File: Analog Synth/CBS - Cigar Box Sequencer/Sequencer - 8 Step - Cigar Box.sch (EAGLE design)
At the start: 117 parts, among them IC1 TL084P, IC10 79L05, IC2 TL084P, IC3 TL084P, IC4 74AC138N, IC5 4050N, IC6 78L05, IC7 40193N, IC8 78L05, Q1 I/O, Q2 I/O, Q3 I/O, X1 I/O, X2 I/O, X3 I/O

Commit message: CBS - still working on Cigar Box Sequencer schematic
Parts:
- added IC9: 74LS86N, 74xx-us:74LS86N
- added Q4: 2N3906, transistor-pnp:2N3906
- added R19, R20, R21: 47k, rcl:R-US_R0603
- added R22, R23, R24, R25: 10k, rcl:R-US_R0603
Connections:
- new net -5V_LEDS: Q4.E
- new net INTERNAL_RESET: IC9B.I1
- new net N$41: Q4.B, R19.1, R20.2
- new net N$42: IC7G$1.CLEAR, IC9B.O
- new net N$43: IC5F.I, R21.1
- new net N$44: LED-INT-OSC.C, R22.2
- new net N$45: CLK-SOURCE.B1, IC5F.O, IC9A.I0, LED-INT-OSC.A
- new net N$46: CLK-SOURCE.A, CLK-SOURCE.B, IC9C.I0
- new net N$47: CLK-SOURCE.B2, IC9A.O
- new net N$48: CLK-SOURCE.A3, LED-EXTERNAL.A
- new net N$49: CLK-SOURCE.A2, LED-INT+EXT.A
- new net N$50: CLK-SOURCE.A1, LED-INTERNAL.A
- new net N$51: LED-INTERNAL.C, R23.2
- new net N$52: LED-INT+EXT.C, R24.2
- new net N$53: LED-EXTERNAL.C, R25.2
- new net N$54: R21.2
- new net N$55: IC7G$1.UP, IC9C.O
- new net N$56: IC9C.I1
- net +5V: now also FREQ-MANUAL.E
- net -12V: now also Q4.C, R20.1
- net -5V: now also FREQ-MANUAL.A
- net 5V_DIGITAL: now also IC7P.VDD, IC9P.VCC
- net GND: now also IC7G$1.A, IC7G$1.B, IC7G$1.C, IC7G$1.D, IC7G$1.LOAD, IC9P.GND, R19.2, R22.1, R23.1, R24.1, R25.1; no longer X1.P3, X2.P3, X3.P3
- net N$1: now also LED-FREQ-CV.A
- net N$10: now also IC9B.I0
- net N$25: now also CLK-SOURCE.B3, IC9A.I1
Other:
- moved on the sheet: C4, C5, CV-OUT, FREQ-CV, FREQ-MANUAL, FREQ-RANGE, IC1A, IC4, IC5F, IC7, IC7P, LED-EXTERNAL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

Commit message: CBS - still working through Cigar Box Sequencer details
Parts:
- added R26, R27, R30, R32: 1k, rcl:R-US_R0603
- added R31, R33, R34, R35: 10k, rcl:R-US_R0603
- R19: value 47k -> 33k
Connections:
- net N$11 renamed X3
- net N$23 renamed X2
- net N$24 renamed X1
- removed net -5V_LEDS: Q4.E
- new net LED_SUPPLY: LED-FREQ-CV.C, Q4.E
- new net N$11: Q1.P2, R26.2
- new net N$23: Q2.P2, R27.2
- new net N$24: Q3.P2, R30.2
- new net N$61: LED-CLK-OUT.C, R31.2
- new net N$62: LED-Q1.C, R33.2
- new net N$63: LED-Q2.C, R34.2
- new net N$64: LED-Q3.C, R35.2
- new net Q1: IC7G$1.QA, LED-Q1.A, R26.1, X1.P3
- new net Q2: IC7G$1.QB, LED-Q2.A, R27.1, X2.P3
- new net Q3: IC7G$1.QC, LED-Q3.A, R30.1, X3.P3
- net GND: now also CLK-OUT.P$1, Q1.P$1, Q2.P$1, Q3.P$1, R31.1, R33.1, R34.1, R35.1
- net N$55: now also LED-CLK-OUT.A, R32.1
- net N$56: now also CLK-OUT.P2, R32.2; no longer IC9C.I1
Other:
- moved on the sheet: CLK-IN, CLK-OUT, CLK-SOURCE, IC7, IC7P, IC9C, LED-EXTERNAL, LED-INT+EXT, LED-INTERNAL, Q1, Q2, Q3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

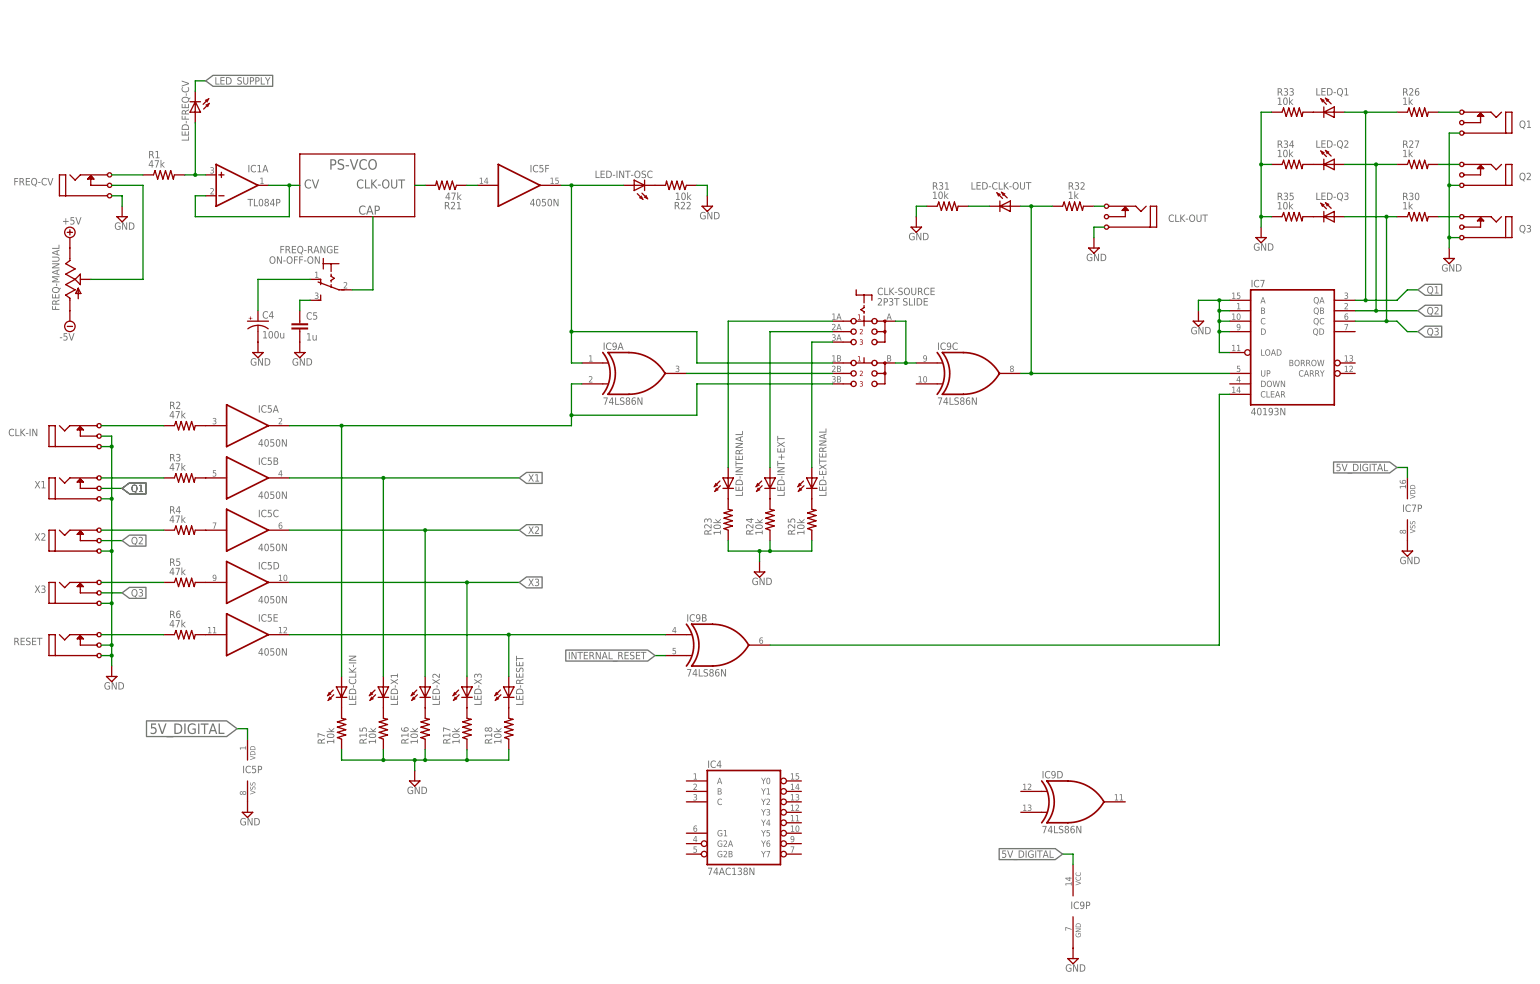
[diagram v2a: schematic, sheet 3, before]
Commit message: CBS: still working on schematic. I need to make sure I understand how I thought this was supposed to work BEFORE I start soldering things together
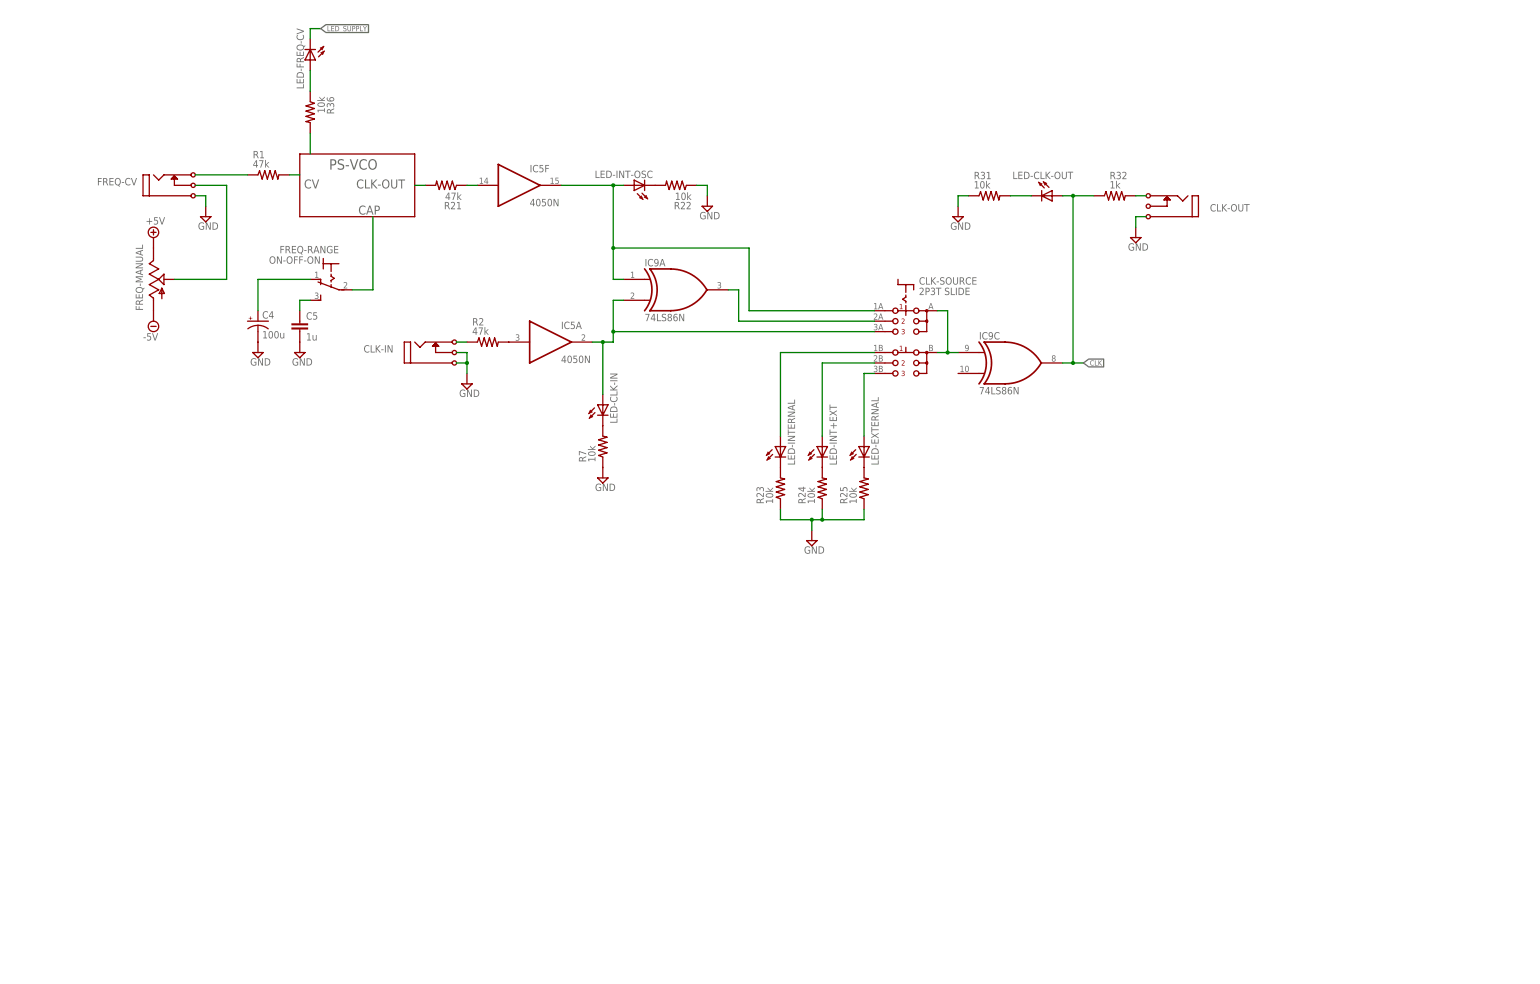
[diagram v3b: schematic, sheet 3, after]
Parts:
- added IC12: 74AC138N, 74xx-eu:74AC138N
- added IC13: 74ALS04N, 74xx-us:74ALS04N
- added R36, R37, R38, R39, R40, R41, R42, R43, R44: 10k, rcl:R-US_R0603
- added S11: STEP-DOWN, switch:5501
- added S9: STEP-UP, switch:5501
- IC4: value 74AC138N -> 74ALS04N; device 74xx-eu:74AC138N -> 74xx-us:74ALS04N
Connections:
- removed net 5V_DIGITAL: C2.+, C3.1, IC5P.VDD, IC6.OUT, IC7P.VDD, IC9P.VCC
- removed net N$47: CLK-SOURCE.B2, IC9A.O
- new net 5V_D: C2.+, C3.1, IC12A.G1, IC12P.VCC, IC13P.VCC, IC4P.VCC, IC5P.VDD, IC6.OUT, IC7P.VDD
- new net CLK: IC9C.O, IC9D.I0, LED-CLK-OUT.A, R32.1
- new net CLK_MAN_DOWN: IC7G$1.DOWN
- new net CLK_MAN_UP: IC9D.I1
- new net N$57: LED-FREQ-CV.A, R36.1
- new net N$58: IC12A.Y3, IC4D.I
- new net N$59: IC12A.Y4, IC4E.I
- new net N$60: IC12A.Y2, IC4C.I
- new net N$65: IC12A.Y1, IC4B.I
- new net N$66: IC12A.Y0, IC4A.I
- new net N$67: IC12A.Y5, IC4F.I
- new net N$68: IC12A.Y6, IC13A.I
- new net N$69: IC12A.Y7, IC13B.I
- new net N$70: CLK-SOURCE.A2, IC9A.O
- new net N$78: LED-S1.C, R37.2
- new net N$79: LED-S2.C, R38.2
- new net N$80: LED-S3.C, R39.2
- new net N$81: LED-S4.C, R40.2
- new net N$82: LED-S5.C, R41.2
- new net N$83: LED-S6.C, R42.2
- new net N$84: LED-S7.C, R43.2
- new net N$85: LED-S8.C, R44.2
- new net S1: IC4A.O, LED-S1.A
- new net S2: IC4B.O, LED-S2.A
- new net S3: IC4C.O, LED-S3.A
- new net S4: IC4D.O, LED-S4.A, S10.11
- new net S5: IC4E.O, LED-S5.A, S10.21
- new net S6: IC4F.O, LED-S6.A, S10.31
- new net S7: IC13A.O, LED-S7.A, S10.41
- new net S8: IC13B.O, LED-S8.A, S10.51
- net GND: now also IC12A.G2A, IC12A.G2B, IC12P.GND, IC13P.GND, IC4P.GND, R37.1, R38.1, R39.1, R40.1, R41.1, R42.1, R43.1, R44.1, S10.61; no longer IC9P.GND
- net INTERNAL_RESET: now also S10.S1
- net N$1: now also R36.2; no longer IC1A.+IN, LED-FREQ-CV.A, R1.2
- net N$25: now also CLK-SOURCE.A3; no longer CLK-SOURCE.B3
- net N$3: now also R1.2; no longer IC1A.-IN, IC1A.OUT
- net N$45: now also CLK-SOURCE.A1; no longer CLK-SOURCE.B1
- net N$48: now also CLK-SOURCE.B3; no longer CLK-SOURCE.A3
- net N$49: now also CLK-SOURCE.B2; no longer CLK-SOURCE.A2
- net N$50: now also CLK-SOURCE.B1; no longer CLK-SOURCE.A1
- net N$55: now also IC9D.O; no longer IC9C.O, LED-CLK-OUT.A, R32.1
- net X1: now also IC12A.A
- net X2: now also IC12A.B
- net X3: now also IC12A.C
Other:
- note added: "+5V Supply for Analog"
- note added: "-4.2 V Supply for LEDs"
- note added: "-5V Supply for Analog"
- note added: "Digital 5V Supply"
- moved on the sheet: C1, C2, C3, CLK-IN, CLK-OUT, CLK-SOURCE, FREQ-CV, FREQ-MANUAL, IC5A, IC6, IC9A, IC9C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

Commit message: CBS: working on skiimatic
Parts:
- removed R38, R39, R40, R41, R42, R43, R44: 10k, rcl:R-US_R0603
- removed S11: STEP-DOWN, switch:5501
- added C6: 0.1u, resistor:C-EU025-050X050
- added C7: 1n, resistor:C-EU025-050X050
- added IC11: MCP6002, linear:MCP602P
- added Q10, Q11, Q12, Q13, Q6, Q7, Q8, Q9: J310, transistor-small-signal:J310
- added Q5: 2N3904, transistor-npn:2N3904
- added R45, R48: 100k, resistor:R-US_0204/7
- added R46: 220k, resistor:R-US_0204/7
- added R47: 47k, resistor:R-US_0204/7
- added R49: 10k, resistor:R-US_0204/7
- added R50, R51, R52, R53, R54, R55, R56, R57: 1M, resistor:R-US_0204/7
- added R58, R59, R60, R61, R62, R63, R64, R65: 1k, resistor:R-US_0204/7
- added U$3: DIODE-0204/5, !synth_sch:DIODE-0204/5
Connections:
- removed net CLK_MAN_DOWN: IC7G$1.DOWN
- removed net N$78: LED-S1.C, R37.2
- removed net N$79: LED-S2.C, R38.2
- removed net N$80: LED-S3.C, R39.2
- removed net N$81: LED-S4.C, R40.2
- removed net N$82: LED-S5.C, R41.2
- removed net N$83: LED-S6.C, R42.2
- removed net N$84: LED-S7.C, R43.2
- removed net N$85: LED-S8.C, R44.2
- new net CLK_MAN_UP_FLT: IC9D.I1
- new net N$47: C6.2, IC11A.+IN, Q5.C, S9.1A, S9.1B
- new net N$71: LED-S1.C, LED-S2.C, LED-S3.C, LED-S4.C, LED-S5.C, LED-S6.C, LED-S7.C, LED-S8.C, R37.2
- new net N$72: Q5.E, R46.2
- new net N$74: C7.2, R49.1
- new net N$75: IC11A.-IN, Q5.B, R47.2, R48.1
- net 5V_D: now also IC11P.V+, IC7G$1.DOWN, IC7G$1.LOAD, R48.2, S9.NC, S9.NO
- net CLK_MAN_UP: now also IC11A.OUT, R49.2; no longer IC9D.I1
- net GND: now also C6.1, C7.1, IC11P.V-, R46.1, R47.1; no longer IC7G$1.LOAD, R38.1, R39.1, R40.1, R41.1, R42.1, R43.1, R44.1
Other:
- note added: "+5 V Supply for Analog"
- note added: "-5 V Supply for Analog"
- note added: "Decoupling capacitors should be placed on the digital 5 V supply close to each digital logic chip."
- note added: "Digital 5 V Supply"
- note removed: "+5V Supply for Analog"
- note removed: "-5V Supply for Analog"
- note removed: "Digital 5V Supply"

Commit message: CBS: schematic (still)
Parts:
- removed Q10, Q11, Q12, Q13, Q7, Q8, Q9: J310, transistor-small-signal:J310
- added C11: 0.1u, resistor:C-EU025-050X050
- added C8: 10u, rcl:CPOL-USE3.5-10
- added IC14: 74AC138N, 74xx-eu:74AC138N
- added IC15, IC16: 74ALS04N, 74xx-us:74ALS04N
- added Q14, Q15, Q16, Q17, Q18, Q19, Q20: J310, transistor-small-signal:J310
- added R38, R39, R40, R41, R42, R43, R44, R66: 1k, resistor:R-US_0204/7
- added R67: 10k, rcl:R-US_R0603
- R36: value 10k -> 2.2k
- R45: value 100k -> 10k
- R50: value 1M -> 2.2k; device resistor:R-US_0204/7 -> rcl:R-US_R0603
- R51, R52, R53, R54, R55, R56: value 1M -> 10k; device resistor:R-US_0204/7 -> rcl:R-US_R0603
- R58, R59, R60, R61, R62, R63, R64: value 1k -> 1M
- R65: value 1k -> 10k; device resistor:R-US_0204/7 -> rcl:R-US_R0603
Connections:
- new net CV_UNBUF: IC1A.+IN, Q14.S, Q15.S, Q16.S, Q17.S, Q18.S, Q19.S, Q20.S, Q6.S
- new net N$100: Q17.G, R61.2, U$5.ANODE
- new net N$101: Q17.D, R42.1, R61.1
- new net N$102: Q18.G, R62.2, U$6.ANODE
- new net N$103: Q18.D, R43.1, R62.1
- new net N$104: Q19.G, R63.2, U$7.ANODE
- new net N$105: Q19.D, R44.1, R63.1
- new net N$106: Q20.G, R64.2, U$8.ANODE
- new net N$107: Q20.D, R64.1, R66.1
- new net N$108: CV-OUT.P2, IC1B.-IN, IC1B.OUT, LED-CV-OUT.A
- new net N$109: FILTER-RANGE.P, IC1B.+IN, LOW-PASS.E
- new net N$110: C11.1, FILTER-RANGE.O
- new net N$111: C11.2, C8.-
- new net N$112: C8.+, FILTER-RANGE.S
- new net N$113: R51.1, S1.P2
- new net N$114: R52.1, S2.P2
- new net N$115: LED-CV-OUT.C, R50.1
- new net N$116: IC2A.-IN, IC2B.-IN, IC2C.-IN, IC2D.-IN, IC3A.-IN, IC3B.-IN, IC3C.-IN, IC3D.-IN, R45.1, U$9.ANODE
- new net N$117: R53.1, S3.P2
- new net N$118: R54.1, S4.P2
- new net N$119: R55.1, S5.P2
- new net N$120: R56.1, S6.P2
- new net N$121: R65.1, S7.P2
- new net N$122: R67.1, S8.P2
- new net N$123: S1.P$1, S2.P$1, S3.P$1, S4.P$1, S5.P$1, S6.P$1, S7.P$1, S8.P$1
- new net N$73: IC1A.-IN, IC1A.OUT, LOW-PASS.A, LOW-PASS.S
- new net N$76: IC3D.OUT, U$8.CATHODE
- new net N$77: IC3C.OUT, U$7.CATHODE
- new net N$78: IC3B.OUT, U$6.CATHODE
- new net N$79: IC3A.OUT, U$5.CATHODE
- new net N$80: IC2D.OUT, U$4.CATHODE
- new net N$81: IC2C.OUT, U$3.CATHODE
- new net N$82: IC2B.OUT, U$2.CATHODE
- new net N$83: IC2A.OUT, U$1.CATHODE
- new net N$84: P1.S, R38.2
- new net N$85: P2.S, R39.2
- new net N$86: P3.S, R40.2
- new net N$87: P4.S, R41.2
- new net N$88: P5.S, R42.2
- new net N$89: P6.S, R43.2
- new net N$90: P7.S, R44.2
- new net N$91: P8.S, R66.2
- new net N$92: Q6.G, R57.2, U$1.ANODE
- new net N$93: Q6.D, R38.1, R57.1
- new net N$94: Q14.G, R58.2, U$2.ANODE
- new net N$95: Q14.D, R39.1, R58.1
- new net N$96: Q15.G, R59.2, U$3.ANODE
- new net N$97: Q15.D, R40.1, R59.1
- new net N$98: Q16.G, R60.2, U$4.ANODE
- new net N$99: Q16.D, R41.1, R60.1
- net +5V: now also P1.E, P2.E, P3.E, P4.E, P5.E, P6.E, P7.E, P8.E
- net -5V: now also C21.2, P1.A, P2.A, P3.A, P4.A, P5.A, P6.A, P7.A, P8.A; no longer C21.1
- net 5V_D: now also IC11B.-IN, IC14A.G1, R45.2; no longer IC12A.G1
- net GND: now also C21.1, CV-OUT.P$1, IC11B.+IN, IC14A.G2A, IC14A.G2B, U$9.CATHODE; no longer C21.2, IC12A.G2A, IC12A.G2B
- net LED_SUPPLY: now also R50.2
- net N$58: now also IC14A.Y3, IC15D.I; no longer IC12A.Y3, IC4D.I
- net N$59: now also IC14A.Y4, IC15E.I; no longer IC12A.Y4, IC4E.I
- net N$60: now also IC14A.Y2, IC15C.I; no longer IC12A.Y2, IC4C.I
- net N$65: now also IC14A.Y1, IC15B.I; no longer IC12A.Y1, IC4B.I
- net N$66: now also IC14A.Y0, IC15A.I; no longer IC12A.Y0, IC4A.I
- net N$67: now also IC14A.Y5, IC15F.I; no longer IC12A.Y5, IC4F.I
- net N$68: now also IC14A.Y6, IC16A.I; no longer IC12A.Y6, IC13A.I
- net N$69: now also IC14A.Y7, IC16B.I; no longer IC12A.Y7, IC13B.I
- net S1: now also IC15A.O, IC2A.+IN, R51.2; no longer IC4A.O
- net S2: now also IC15B.O, IC2B.+IN, R52.2; no longer IC4B.O
- net S3: now also IC15C.O, IC2C.+IN, R53.2; no longer IC4C.O
- net S4: now also IC15D.O, IC2D.+IN, R54.2; no longer IC4D.O
- net S5: now also IC15E.O, IC3A.+IN, R55.2; no longer IC4E.O
- net S6: now also IC15F.O, IC3B.+IN, R56.2; no longer IC4F.O
- net S7: now also IC16A.O, IC3C.+IN, R65.2; no longer IC13A.O
- net S8: now also IC16B.O, IC3D.+IN, R67.2; no longer IC13B.O
- net X1: now also IC14A.A; no longer IC12A.A
- net X2: now also IC14A.B; no longer IC12A.B
- net X3: now also IC14A.C; no longer IC12A.C

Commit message: CBS: schematic (stillstill)
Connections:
- net CLK: no longer IC9C.O
- net N$46: no longer IC9C.I0
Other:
- moved on the sheet: C4, C5, CLK-IN, CLK-OUT, CLK-SOURCE, FREQ-CV, FREQ-MANUAL, FREQ-RANGE, IC5A, IC5F, IC9A, LED-CLK-IN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

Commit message: CBS: added the switches for the GATE output that replaces the clock output
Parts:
- removed CLK-OUT: I/O, !synth_sch:MONO_JACK
- removed LED-CLK-OUT: TLLG4400, led:TLLG4400
- added G1, G2, G3, G4, G5, G6, G7, G8: ON-OFF-ON, switch:320-916
- added GATE_OUT: I/O, !synth_sch:MONO_JACK
- added LED_GATE_OUT: TLLG4400, led:TLLG4400
- added R68: 10k, rcl:R-US_R0603
- added U$11, U$12, U$14, U$15, U$16, U$17, U$18, U$19: DIODE-0204/5, !synth_sch:DIODE-0204/5
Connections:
- new net COMBINED-GATE-SIGNAL-AFAEVIRO: IC16F.O, LED_GATE_OUT.A, R32.1
- new net N$124: IC16E.O, IC16F.I
- new net N$133: G1.O, U$11.ANODE
- new net N$134: G2.O, U$12.ANODE
- new net N$135: G3.O, U$14.ANODE
- new net N$136: G4.O, U$15.ANODE
- new net N$137: G5.O, U$16.ANODE
- new net N$138: G6.O, U$17.ANODE
- new net N$139: G7.O, U$18.ANODE
- new net N$140: G8.O, U$19.ANODE
- new net N$141: IC16E.I, R68.2, U$11.CATHODE, U$12.CATHODE, U$14.CATHODE, U$15.CATHODE, U$16.CATHODE, U$17.CATHODE, U$18.CATHODE, U$19.CATHODE
- net CLK: no longer LED-CLK-OUT.A, R32.1
- net GND: now also GATE_OUT.P$1, R68.1; no longer CLK-OUT.P$1
- net N$56: now also GATE_OUT.P2; no longer CLK-OUT.P2
- net N$61: now also LED_GATE_OUT.C; no longer LED-CLK-OUT.C
- net S1: now also G1.P
- net S2: now also G2.P
- net S3: now also G3.P
- net S4: now also G4.P
- net S5: now also G5.P
- net S6: now also G6.P
- net S7: now also G7.P
- net S8: now also G8.P
